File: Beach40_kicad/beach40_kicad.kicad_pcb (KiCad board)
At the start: 2 copper layers, 29 parts, among them Q1 2N2222, Q2 BD139

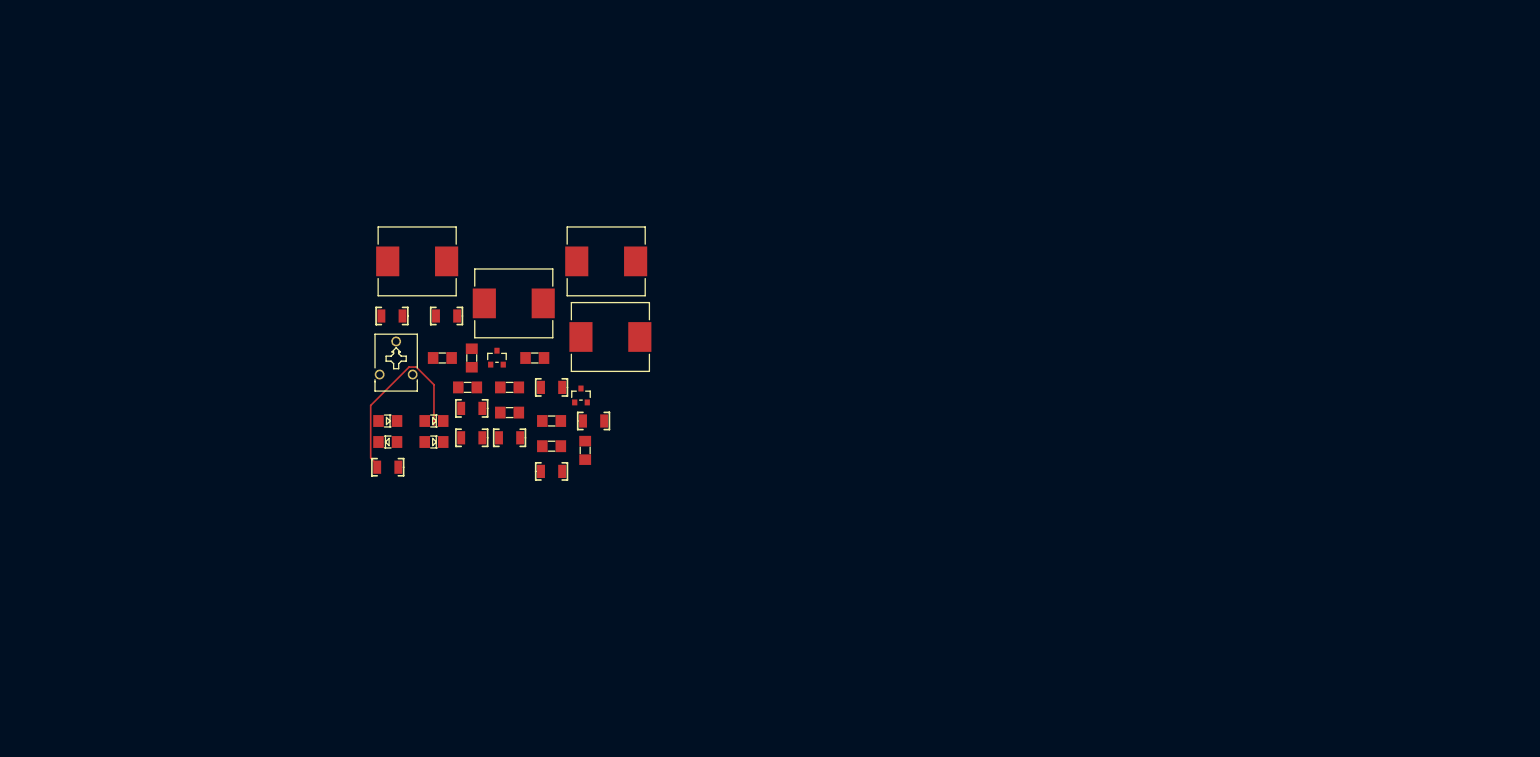
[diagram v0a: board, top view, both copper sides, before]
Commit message: first proper go of the board layout, still missing footrprints, and some nets!
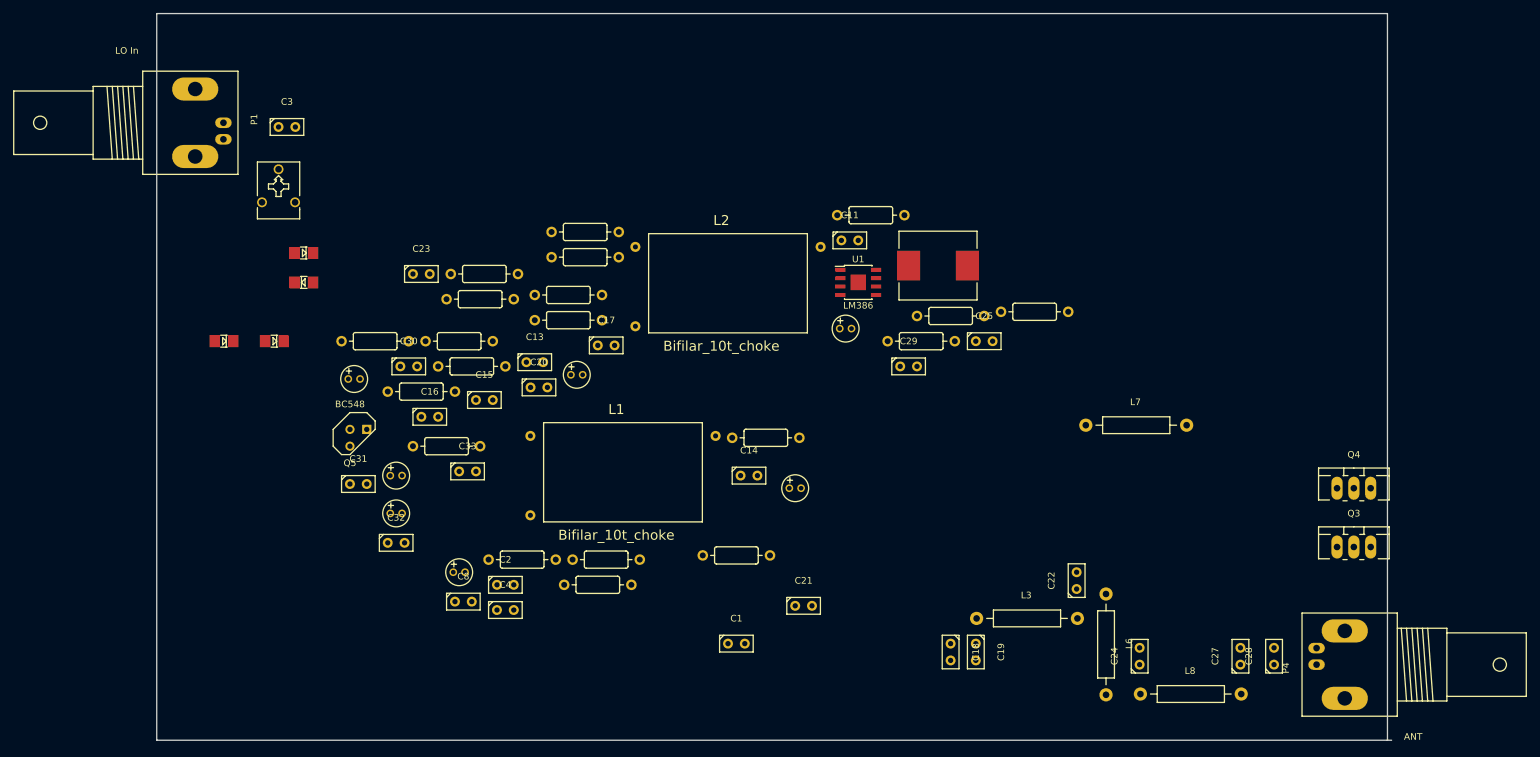
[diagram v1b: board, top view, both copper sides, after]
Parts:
- removed L4: 10t BiFilar, FT:IND_SRP1040
- removed Q1: 2N2222, FT:SOT23_TRANSISTOR
- removed Q2: BD139, FT:SOT23_TRANSISTOR
- added C10: 220u, FT:CAP_ELECTRO_D4S1.8, F.Cu at (176.5, 101.6)
- added C11: 47u, Capacitors_ThroughHole:Capacitor3MMDiscRM2.5, F.Cu at (177.2, 88.3)
- added C12: 220u, FT:CAP_ELECTRO_D4S1.8, F.Cu at (135.9, 108.6)
- added C13: 4.7n, Capacitors_ThroughHole:Capacitor3MMDiscRM2.5, F.Cu at (129.5, 106.7)
- added C14: 100n, Capacitors_ThroughHole:Capacitor3MMDiscRM2.5, F.Cu at (161.9, 123.8)
- added C15: 1n, Capacitors_ThroughHole:Capacitor3MMDiscRM2.5, F.Cu at (121.9, 112.4)
- added C16: 100n, Capacitors_ThroughHole:Capacitor3MMDiscRM2.5, F.Cu at (113.7, 114.9)
- added C17: 100n, Capacitors_ThroughHole:Capacitor3MMDiscRM2.5, F.Cu at (140.3, 104.1)
- added C18: 220p, Capacitors_ThroughHole:Capacitor3MMDiscRM2.5, F.Cu at (192.4, 150.5)
- added C19: 220p, Capacitors_ThroughHole:Capacitor3MMDiscRM2.5, F.Cu at (196.2, 150.5)
- added C20: 100n, Capacitors_ThroughHole:Capacitor3MMDiscRM2.5, F.Cu at (130.2, 110.5)
- added C21: 100n, Capacitors_ThroughHole:Capacitor3MMDiscRM2.5, F.Cu at (170.2, 143.5)
- added C22: 820p, Capacitors_ThroughHole:Capacitor3MMDiscRM2.5, F.Cu at (211.5, 139.7)
- added C23: 100n, Capacitors_ThroughHole:Capacitor3MMDiscRM2.5, F.Cu at (112.4, 93.3)
- added C24: 820p, Capacitors_ThroughHole:Capacitor3MMDiscRM2.5, F.Cu at (221.0, 151.1)
- added C25: 100n, Capacitors_ThroughHole:Capacitor3MMDiscRM2.5, F.Cu at (197.5, 103.5)
- added C26: 220u, FT:CAP_ELECTRO_D4S1.8, F.Cu at (108.6, 129.5)
- added C27: 220p, Capacitors_ThroughHole:Capacitor3MMDiscRM2.5, F.Cu at (236.2, 151.1)
- added C28: 220p, Capacitors_ThroughHole:Capacitor3MMDiscRM2.5, F.Cu at (241.3, 151.1)
- added C29: 100n, Capacitors_ThroughHole:Capacitor3MMDiscRM2.5, F.Cu at (186.1, 107.3)
- added C30: 100n, Capacitors_ThroughHole:Capacitor3MMDiscRM2.5, F.Cu at (110.5, 107.3)
- added C31: 1n, Capacitors_ThroughHole:Capacitor3MMDiscRM2.5, F.Cu at (102.9, 125.1)
- added C32: 100n, Capacitors_ThroughHole:Capacitor3MMDiscRM2.5, F.Cu at (108.6, 134.0)
- added C33: 18p, Capacitors_ThroughHole:Capacitor3MMDiscRM2.5, F.Cu at (119.4, 123.2)
- added L6: 1u, Choke_Axial_ThroughHole:Choke_Horizontal_RM15mm, F.Cu at (215.9, 149.2)
- added L7: 1u, Choke_Axial_ThroughHole:Choke_Horizontal_RM15mm, F.Cu at (220.3, 116.2)
- added L8: 1u, Choke_Axial_ThroughHole:Choke_Horizontal_RM15mm, F.Cu at (228.6, 156.8)
- added L9: 3T FB, FT:IND_SRP1040, F.Cu at (190.5, 92.1)
- added P1: LO In, Sockets_BNC:BNC_Socket_TYCO-AMP_LargePads, F.Cu at (77.5, 70.5)
- added P4: ANT, Sockets_BNC:BNC_Socket_TYCO-AMP_LargePads, F.Cu at (252.7, 152.4)
- added Q3: BD139, Transistors_TO-220:TO-220_Bipolar-BCE_Vertical_LargePads, F.Cu at (253.4, 134.6)
- added Q4: BD139, Transistors_TO-220:TO-220_Bipolar-BCE_Vertical_LargePads, F.Cu at (253.4, 125.7)
- added Q5: BC548, Discret:TO92, F.Cu at (102.9, 118.1)
- added R10: 2.2k, FT:RES_AXIAL_400MIL, F.Cu at (116.2, 119.4)
- added R11: 1k1, FT:RES_AXIAL_400MIL, F.Cu at (112.4, 111.1)
- added R12: 100, FT:RES_AXIAL_400MIL, F.Cu at (121.3, 97.2)
- added R13: 10, FT:RES_AXIAL_400MIL, F.Cu at (134.6, 96.5)
- added R14: 470, FT:RES_AXIAL_400MIL, F.Cu at (137.2, 90.8)
- added R15: 2.2k, FT:RES_AXIAL_400MIL, F.Cu at (137.2, 87.0)
- added R16: 22, FT:RES_AXIAL_400MIL, F.Cu at (118.1, 103.5)
- added R17: 4.7, FT:RES_AXIAL_400MIL, F.Cu at (121.9, 93.3)
- added R18: 6.8k, FT:RES_AXIAL_400MIL, F.Cu at (192.4, 99.7)
- added R19: 330, FT:RES_AXIAL_400MIL, F.Cu at (205.1, 99.1)
- added R20: 2.2, FT:RES_AXIAL_400MIL, F.Cu at (120.0, 107.3)
- added U1: LM386, Housings_SOIC:SOIC-8-1EP_3.9x4.9mm_Pitch1.27mm, F.Cu at (178.4, 94.6)
- C1: value 10n -> 100n; footprint FT:1210_CAP -> Capacitors_ThroughHole:Capacitor3MMDiscRM2.5
- C2: value 10nF -> 100n; footprint FT:1210_CAP -> Capacitors_ThroughHole:Capacitor3MMDiscRM2.5
- C3: value 100n -> 10n; footprint FT:1210_CAP -> Capacitors_ThroughHole:Capacitor3MMDiscRM2.5
- C4: footprint FT:1210_CAP -> Capacitors_ThroughHole:Capacitor3MMDiscRM2.5
- C5: value 100n -> 1u; footprint FT:1210_CAP -> FT:CAP_ELECTRO_D4S1.8
- C6: value 100n -> 68p; footprint FT:1210_CAP -> FT:CAP_ELECTRO_D4S1.8
- C7: value 100n -> 4.7u; footprint FT:1210_CAP -> FT:CAP_ELECTRO_D4S1.8
- C8: value 100n -> 10nF; footprint FT:1210_CAP -> Capacitors_ThroughHole:Capacitor3MMDiscRM2.5
- C9: value 100n -> 220u; footprint FT:1210_CAP -> FT:CAP_ELECTRO_D4S1.8
- L1: value 10T BiFilar -> Bifilar_10t_choke; footprint FT:IND_SRP1040 -> custom_chokes:Biflar_10t_choke
- L2: value 10t BiFilar -> Bifilar_10t_choke; footprint FT:IND_SRP1040 -> custom_chokes:Biflar_10t_choke
- L3: value 10t BiFilar -> 1u; footprint FT:IND_SRP1040 -> Choke_Axial_ThroughHole:Choke_Horizontal_RM15mm
- R1: value 100 -> 22k; footprint FT:1206 -> FT:RES_AXIAL_400MIL
- R2: value 2.2k -> 330; footprint FT:1206 -> FT:RES_AXIAL_400MIL
- R3: value 1k1 -> 2.2k; footprint FT:1206 -> FT:RES_AXIAL_400MIL
- R4: footprint FT:1206 -> FT:RES_AXIAL_400MIL
- R5: value 10 -> 220; footprint FT:1206 -> FT:RES_AXIAL_400MIL
- R6: value 470 -> 10; footprint FT:1206 -> FT:RES_AXIAL_400MIL
- R7: value 2.2k -> 18; footprint FT:1206 -> FT:RES_AXIAL_400MIL
- R8: value 22 -> 2.2k; footprint FT:1206 -> FT:RES_AXIAL_400MIL
- R9: value 4.7 -> 100; footprint FT:1206 -> FT:RES_AXIAL_400MIL
- moved L3 83.3 mm to (203.8, 145.4)
- moved C1 71.9 mm to (160.0, 149.2)
- moved R6 58.1 mm to (188.0, 103.5)
- moved R7 55.2 mm to (180.3, 84.5)
- moved R2 49.9 mm to (160.0, 135.9), turned to 180 degrees
- moved L1 44.9 mm to (142.9, 123.8)
- moved R1 39.3 mm to (140.3, 136.5), turned to 180 degrees
- moved C3 37.4 mm to (92.1, 71.1)
- moved R3 35.8 mm to (139.1, 140.3), turned to 0 degrees
- moved D1 34.7 mm to (94.6, 90.2)
- moved L2 32.5 mm to (158.8, 95.2)
- moved C7 32.1 mm to (168.9, 125.7), turned to 0 degrees
- moved VR1 31.5 mm to (90.8, 80.0)
- moved C6 29.9 mm to (102.2, 109.2)
- moved R5 29.3 mm to (105.4, 103.5)
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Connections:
- C1 pad 1: Net-(C1-Pad1) -> GND
- C2 pad 1: Audio -> Net-(C2-Pad1)
- C2 pad 2: GND -> Net-(C2-Pad2)
- C3 pad 2: GND -> Net-(C3-Pad2)
- C4 pad 1: LPF -> Net-(C2-Pad1)
- C4 pad 2: Net-(4:1-Pad4) -> GND
- C5 pad 2: Net-(4:1-Pad4) -> Audio
- C7 pad 2: Net-(C7-Pad2) -> Audio
- C8 pad 1: +12V -> Audio
- C9 pad 1: Net-(C9-Pad1) -> T/R-P-NC
- D3 pad A: Net-(D3-PadA) -> GND
- D4 pad K: Net-(D3-PadA) -> GND
- L1 pad 1: Net-(C3-Pad1) -> Net-(L1-Pad1)
- L1 pad 2: Net-(C7-Pad1) -> Net-(C20-Pad1)
- L2 pad 2: Net-(C3-Pad1) -> Net-(C25-Pad2)
- L3 pad 1: +12V -> LPF
- R1 pad 1: +12V -> Net-(C1-Pad2)
- R1 pad 2: Net-(C3-Pad1) -> Net-(C2-Pad2)
- R2 pad 1: Net-(L2-Pad1) -> T/R-P-NO
- R2 pad 2: Net-(C5-Pad1) -> Net-(C1-Pad2)
- R3 pad 2: GND -> Net-(C1-Pad2)
- R4 pad 1: Net-(Q1-PadE) -> Net-(C5-Pad1)
- R4 pad 2: GND -> Net-(C2-Pad1)
- R5 pad 1: Net-(Q1-PadE) -> Net-(C6-Pad1)
- R5 pad 2: Net-(C6-Pad1) -> GND
- R6 pad 1: Net-(C7-Pad2) -> T/R-P-NC
- R6 pad 2: GND -> Net-(C10-Pad1)
- R7 pad 2: Net-(C7-Pad2) -> GND
- R8 pad 1: Net-(Q2-PadE) -> Net-(C13-Pad2)
- R8 pad 2: GND -> Net-(C11-Pad1)
- R9 pad 1: Net-(Q2-PadE) -> T/R-P-NO
- R9 pad 2: Net-(C9-Pad1) -> Net-(C14-Pad1)
- VR1 pad W: Net-(C1-Pad1) -> Net-(C3-Pad1)
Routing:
- net Audio: track 28.9 -> 0.00 mm
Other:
- board outline added: 186.7 x 109.9 mm

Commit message: reverted a bit, back to SMD components, much more better! Actual start of layout now.
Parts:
- added CAP_TRIM1: 4-40p, Discret:C2, F.Cu at (74.3, 52.7)
- added P2: MIC_IN, Pin_Headers:Pin_Header_Straight_1x02, F.Cu at (208.9, 97.8)
- added P3: Audio Out, Pin_Headers:Pin_Header_Straight_1x02, F.Cu at (233.0, 69.2)
- added PTT1: SW_PUSH, Pin_Headers:Pin_Header_Straight_1x02, F.Cu at (248.3, 138.4)
- added Q1: BC548, Housings_TO-92:TO-92_Inline_Narrow_Oval, F.Cu at (70.5, 74.3)
- added Q2: 2N2222, FT:SOT23_TRANSISTOR, F.Cu at (238.1, 135.9)
- added R21: 100k, FT:1210, F.Cu at (203.2, 135.9)
- added R22: 4.7k, FT:1210, F.Cu at (203.8, 131.4)
- added T1: 4:10_Transformer, custom_chokes:4_10_Transformer, F.Cu at (114.3, 60.3)
- C1, C13, C14, C15, C16, C17, C18, C19, C2, C20, C21, C22, C23, C24, C25, C27, C28, C29, C3, C30, C31, C32, C33, C4: footprint Capacitors_ThroughHole:Capacitor3MMDiscRM2.5 -> FT:1210_CAP
- C11: footprint Capacitors_ThroughHole:Capacitor3MMDiscRM2.5 -> FT:CAP_ELECTRO_D4S1.8
- C8: footprint Capacitors_ThroughHole:Capacitor3MMDiscRM2.5 -> FT:0603_CAP
- L3, L6, L7, L8: footprint Choke_Axial_ThroughHole:Choke_Horizontal_RM15mm -> FT:1206
- Q3, Q4: footprint Transistors_TO-220:TO-220_Bipolar-BCE_Vertical_LargePads -> Discret:TO220_VERT
- Q5: footprint Discret:TO92 -> Housings_TO-92:TO-92_Inline_Narrow_Oval
- R1, R10, R11, R12, R13, R14, R15, R16, R17, R18, R19, R2, R20, R3, R4, R5, R6, R7, R8, R9: footprint FT:RES_AXIAL_400MIL -> FT:1210
- moved C26 139.0 mm to (228.0, 58.4)
- moved C30 136.9 mm to (243.2, 141.0)
- moved C23 128.3 mm to (231.8, 140.3)
- moved R10 123.9 mm to (237.5, 144.8), turned to 0 degrees
- moved C16 121.8 mm to (233.7, 135.9)
- moved C1 119.0 mm to (230.5, 53.3)
- moved R12 113.0 mm to (225.4, 53.3), turned to 0 degrees
- moved Q5 112.1 mm to (214.0, 132.7)
- moved R11 110.4 mm to (217.2, 146.1), turned to 0 degrees
- moved C13 104.5 mm to (226.1, 66.7)
- moved C20 101.0 mm to (228.0, 135.9)
- moved C27 100.6 mm to (243.8, 50.8), turned to 0 degrees
- moved C9 100.6 mm to (208.9, 130.8)
- moved C28 100.4 mm to (238.1, 50.8), turned to 0 degrees
- moved C7 100.1 mm to (89.5, 64.8), turned to 270 degrees
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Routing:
- net Audio: track 0.00 -> 40.7 mm
- net Net-(CAP_TRIM1-Pad2): track 0.00 -> 32.4 mm
- net Net-(D2-PadK): track 0.00 -> 30.4 mm
- net Net-(C7-Pad1): track 0.00 -> 21.6 mm
- net Net-(C5-Pad1): track 0.00 -> 11.7 mm
- net Net-(C3-Pad2): track 0.00 -> 4.20 mm
- net Net-(C3-Pad1): track 0.00 -> 3.52 mm
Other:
- board size 186.7 x 109.9 mm -> 200 x 100 mm

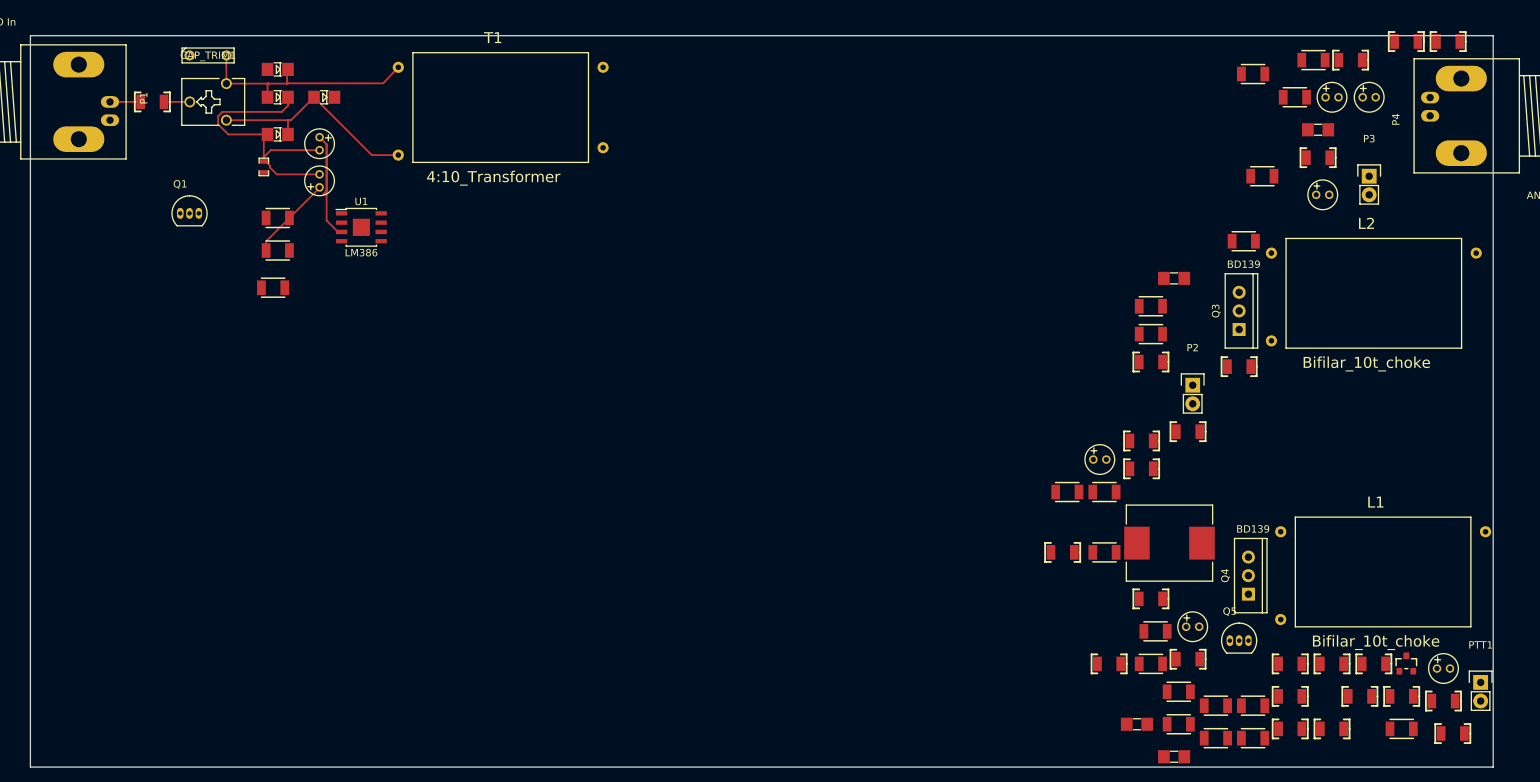
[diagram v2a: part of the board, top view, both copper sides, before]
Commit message: PCB Layout getting there, struggling with Vias.
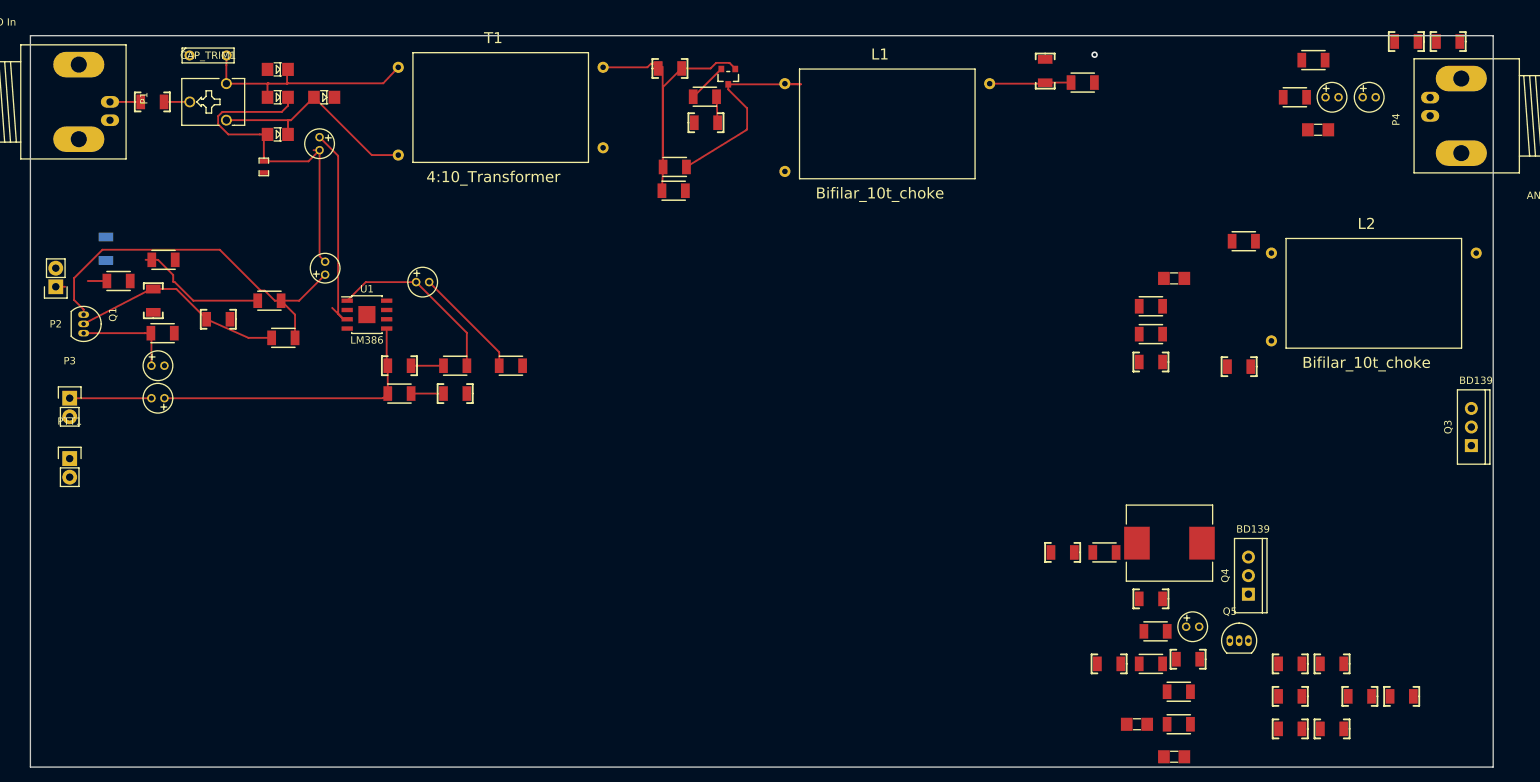
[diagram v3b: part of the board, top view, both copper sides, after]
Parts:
- C1: moved to B.Cu
- moved PTT1 195.3 mm to (55.4, 107.8)
- moved P3 180.2 mm to (55.4, 99.6)
- moved C1 172.1 mm to (60.3, 79.1), turned to 270 degrees
- moved C12 161.7 mm to (67.4, 99.6), turned to 180 degrees
- moved P2 156.0 mm to (53.5, 84.3), turned to 180 degrees
- moved C11 149.2 mm to (103.6, 83.7)
- moved C30 141.5 mm to (108.1, 98.9)
- moved C4 136.5 mm to (66.8, 86.2), turned to 270 degrees
- moved R2 132.9 mm to (62.1, 83.5)
- moved R1 132.5 mm to (68.2, 80.6)
- moved C6 129.4 mm to (67.4, 95.1)
- moved C13 128.8 mm to (100.5, 95.1)
- moved C2 127.9 mm to (75.7, 88.8)
- moved C16 126.1 mm to (137.4, 54.5), turned to 180 degrees
- moved R10 125.6 mm to (138.1, 67.9), turned to 180 degrees
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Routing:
- net Net-(C5-Pad1): track 11.7 -> 51.8 mm
- net Net-(C12-Pad1): track 0.00 -> 39.7 mm
- net Net-(C16-Pad1): track 0.00 -> 39.6 mm
- net Net-(C2-Pad1): track 0.00 -> 29.5 mm
- net Net-(L1-Pad1): track 0.00 -> 29.1 mm
- net Net-(C11-Pad1): track 0.00 -> 24.8 mm
- net Net-(C1-Pad2): track 0.00 -> 18.6 mm
- net Net-(C11-Pad2): track 0.00 -> 15.4 mm
- net Net-(C6-Pad1): track 0.00 -> 13.7 mm
- net Net-(C14-Pad1): track 0.00 -> 11.2 mm
- net Net-(C12-Pad2): track 0.00 -> 11.2 mm
- net Audio: track 40.7 -> 49.2 mm
- net Net-(C15-Pad2): track 0.00 -> 8.09 mm
- net Net-(C7-Pad1): track 21.6 -> 29.4 mm
- net Net-(Q2-PadE): track 0.00 -> 5.42 mm
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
